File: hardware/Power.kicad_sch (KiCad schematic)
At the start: 3 parts, among them U5 BQ25798RQMR

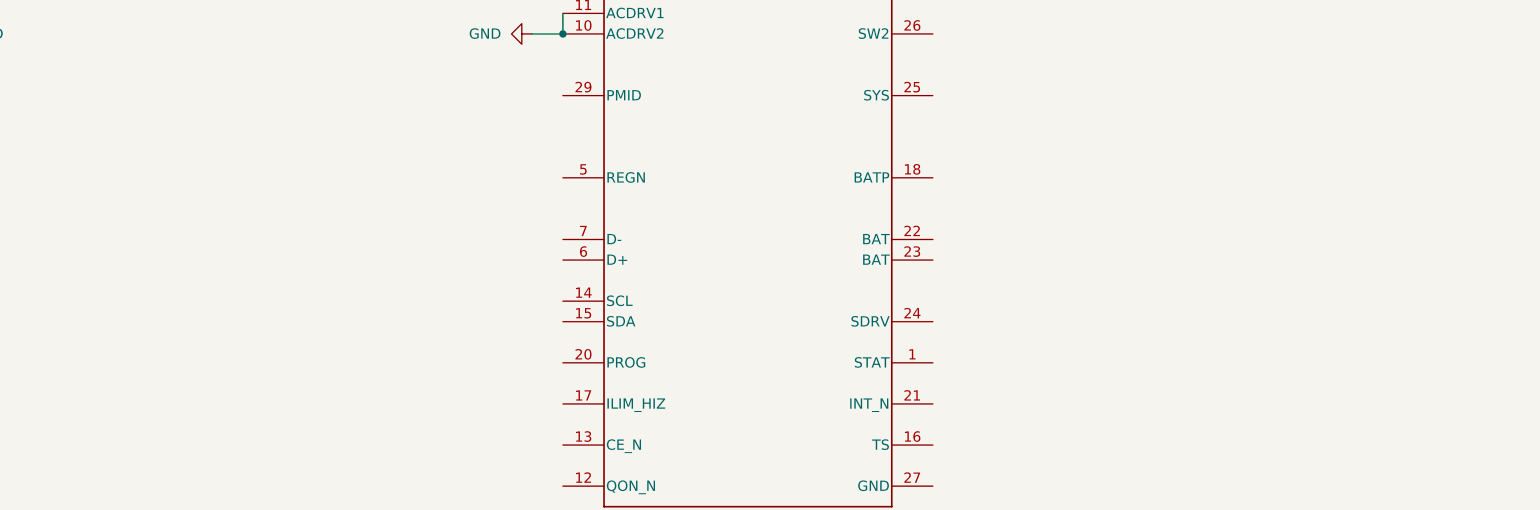
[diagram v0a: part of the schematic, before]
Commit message: Main modules added + Com lines
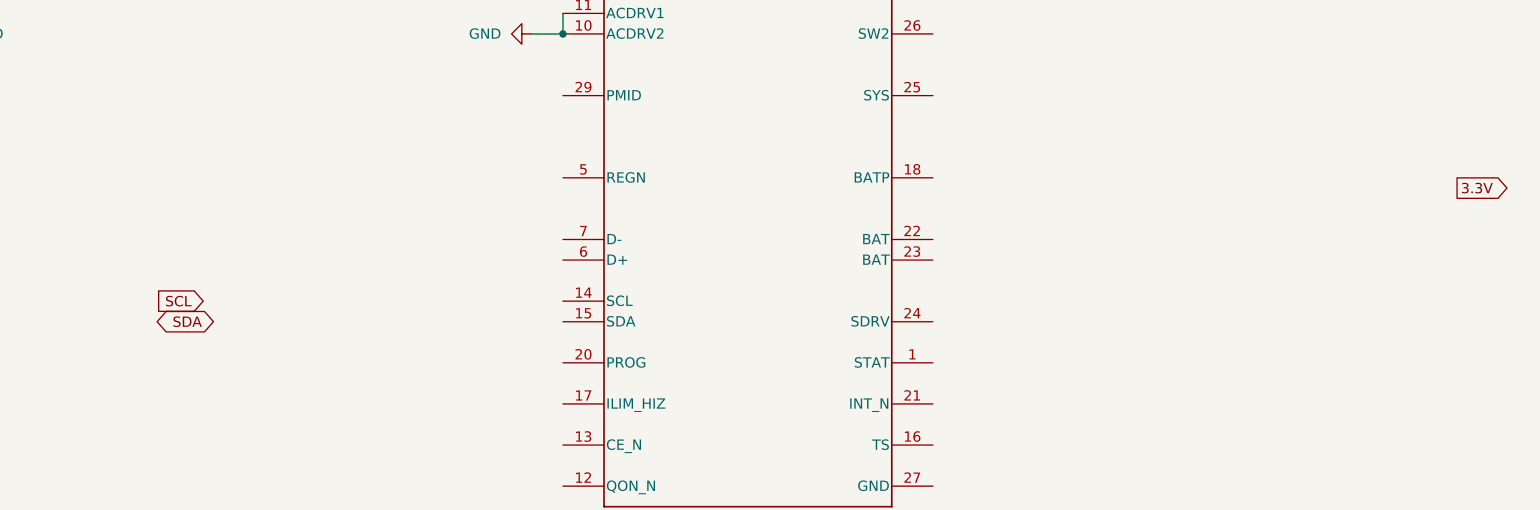
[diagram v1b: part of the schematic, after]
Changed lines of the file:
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@@
+		)
+	)
+	(global_label "3.3V"
+		(shape output)
+		(at 223.52 80.01 0)
+		(fields_autoplaced yes)
+		(effects
+			(font
+				(size 1.27 1.27)
+			)
+			(justify left)
+		)
+		(property "Intersheetrefs" "${INTERSHEET_REFS}"
+			(at 230.6176 80.01 0)
+			(effects
+				(font
+					(size 1.27 1.27)
+				)
+				(justify left)
+				(hide yes)
+			)
 		)
 	)
@@
 			(effects
 				(font
+					(size 1.27 1.27)
+				)
+				(justify right)
+				(hide yes)
+			)
+		)
+	)
+	(global_label "SCL"
+		(shape input)
+		(at 68.58 93.98 180)
+		(fields_autoplaced yes)
+		(effects
+			(font
+				(size 1.27 1.27)
+			)
+			(justify right)
+		)
+		(property "Intersheetrefs" "${INTERSHEET_REFS}"
+			(at 62.0872 93.98 0)
+			(effects
+				(font
+					(size 1.27 1.27)
+				)
+				(justify right)
+				(hide yes)
+			)
+		)
+	)
+	(global_label "SDA"
+		(shape bidirectional)
+		(at 69.85 96.52 180)
+		(fields_autoplaced yes)
+		(effects
+			(font
+				(size 1.27 1.27)
+			)
+			(justify right)
+		)
+		(property "Intersheetrefs" "${INTERSHEET_REFS}"
+			(at 62.1854 96.52 0)
+			(effects
+				(font

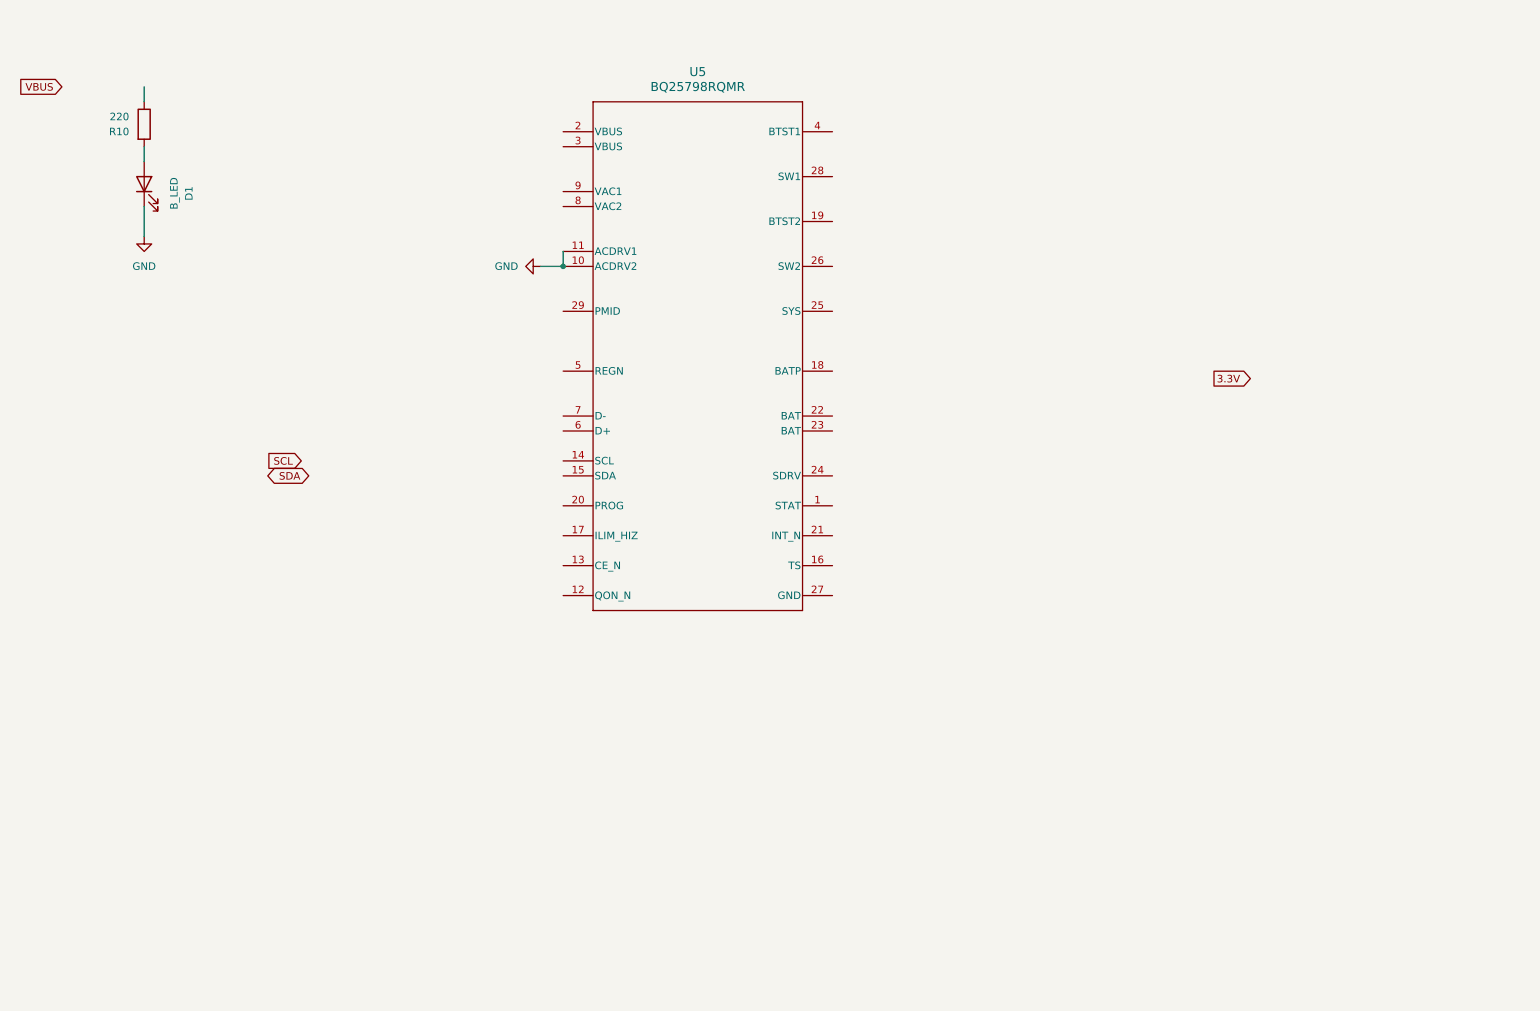
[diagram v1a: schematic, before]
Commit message: Basic 2 inputs source battery charger
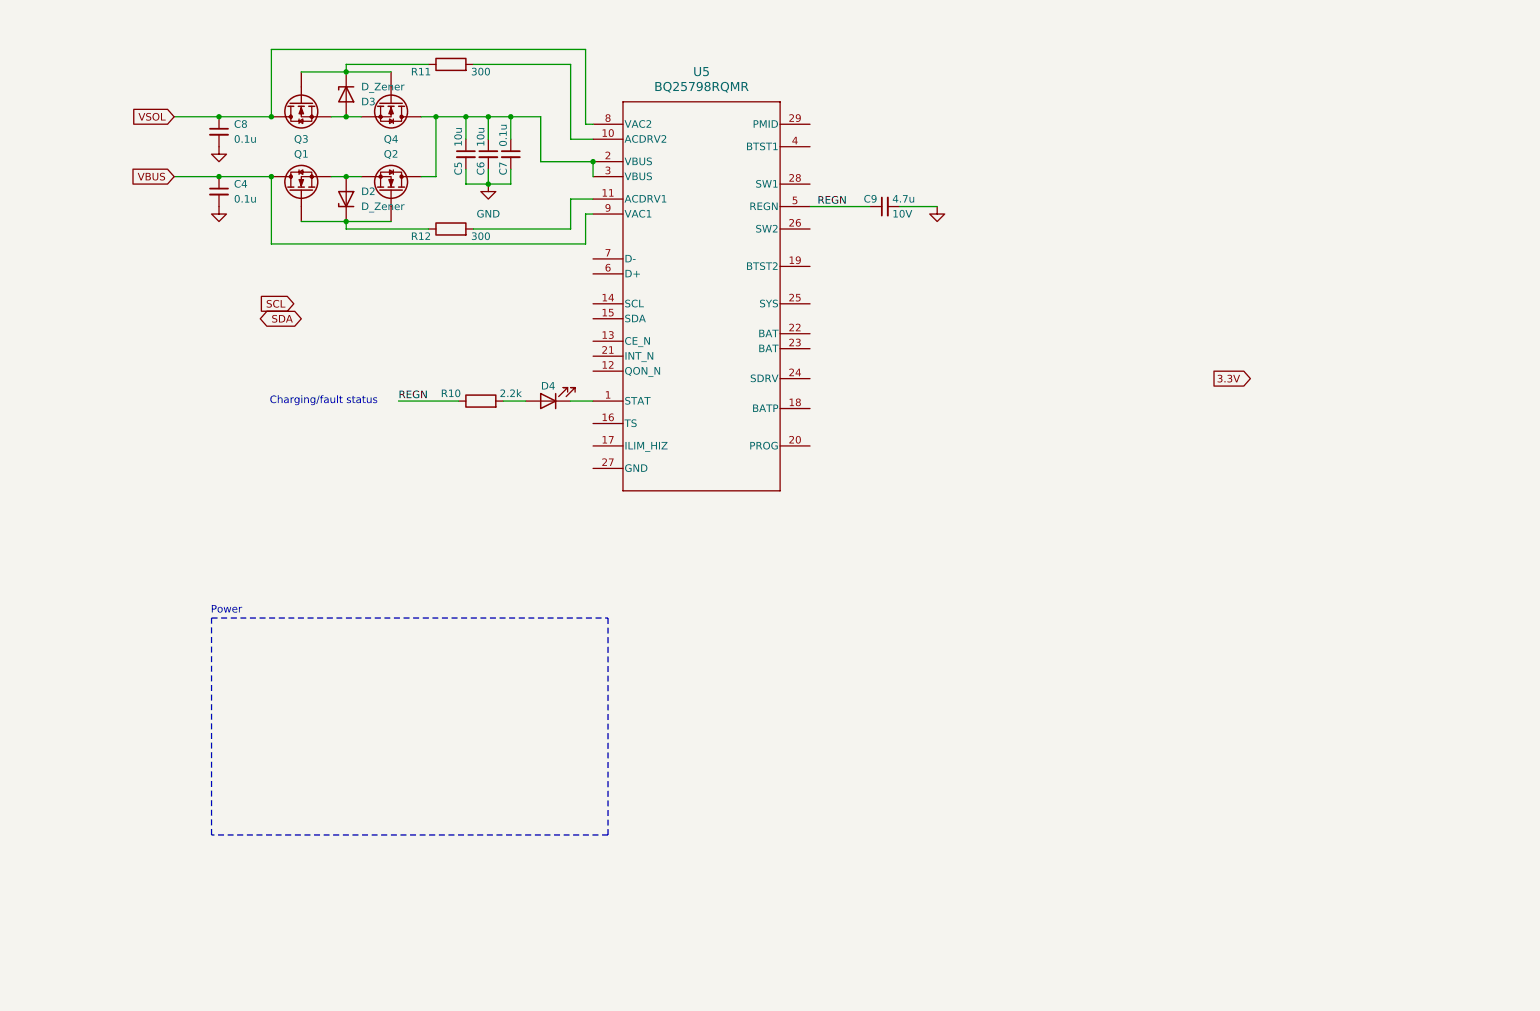
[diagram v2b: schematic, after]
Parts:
- removed D1: B_LED, LED_SMD:LED_0603_1608Metric, symbol Device:LED
- added C4, C7, C8: 0.1u, symbol Device:C_Small
- added C5, C6: 10u, symbol Device:C_Small
- added C9: 4.7u, symbol Device:C_Small
- added D2, D3: D_Zener, symbol Device:D_Zener
- added D4: LED, symbol Device:LED
- added Q1, Q2, Q3, Q4: Q_NMOS, symbol Device:Q_NMOS
- added R11, R12: 300, Resistor_SMD:R_0402_1005Metric, symbol Device:R
- R10: value 220 -> 2.2k; footprint Resistor_SMD:R_0603_1608Metric -> Resistor_SMD:R_0402_1005Metric
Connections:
- net GND: now also C4.2, C5.2, C6.2, C7.2, C8.2, C9.2; no longer U5.10 (ACDRV2), U5.11 (ACDRV1)
- net VBUS: now also U5.9 (VAC1), C4.1, Q1.D
- net at R10.2: now also D4.2 (A)
- net at U5.1 (STAT): now also D4.1 (K)
- net at U5.2 (VBUS): now also U5.3 (VBUS), C5.1, C6.1, C7.1, Q2.D, Q4.D
- net REGN: now reaches U5.5 (REGN)
- net REGN: now also R10.1, C9.1
- net VSOL: now reaches U5.8 (VAC2)
- net VSOL: now also C8.1, Q3.D
- new net: D3.1 (K), Q3.G, Q4.G, R11.1
- new net: D3.2 (A), Q3.S, Q4.S
- new net: D2.1 (K), Q1.G, Q2.G, R12.1
- new net: D2.2 (A), Q1.S, Q2.S
- new net: R11.2, U5.10 (ACDRV2)
- new net: R12.2, U5.11 (ACDRV1)
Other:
- note added: "Charging/fault status"
- note added: "Power"
- company: (none) -> ECAM
- title: (none) -> Power/Battery Management
- moved on the sheet: R10

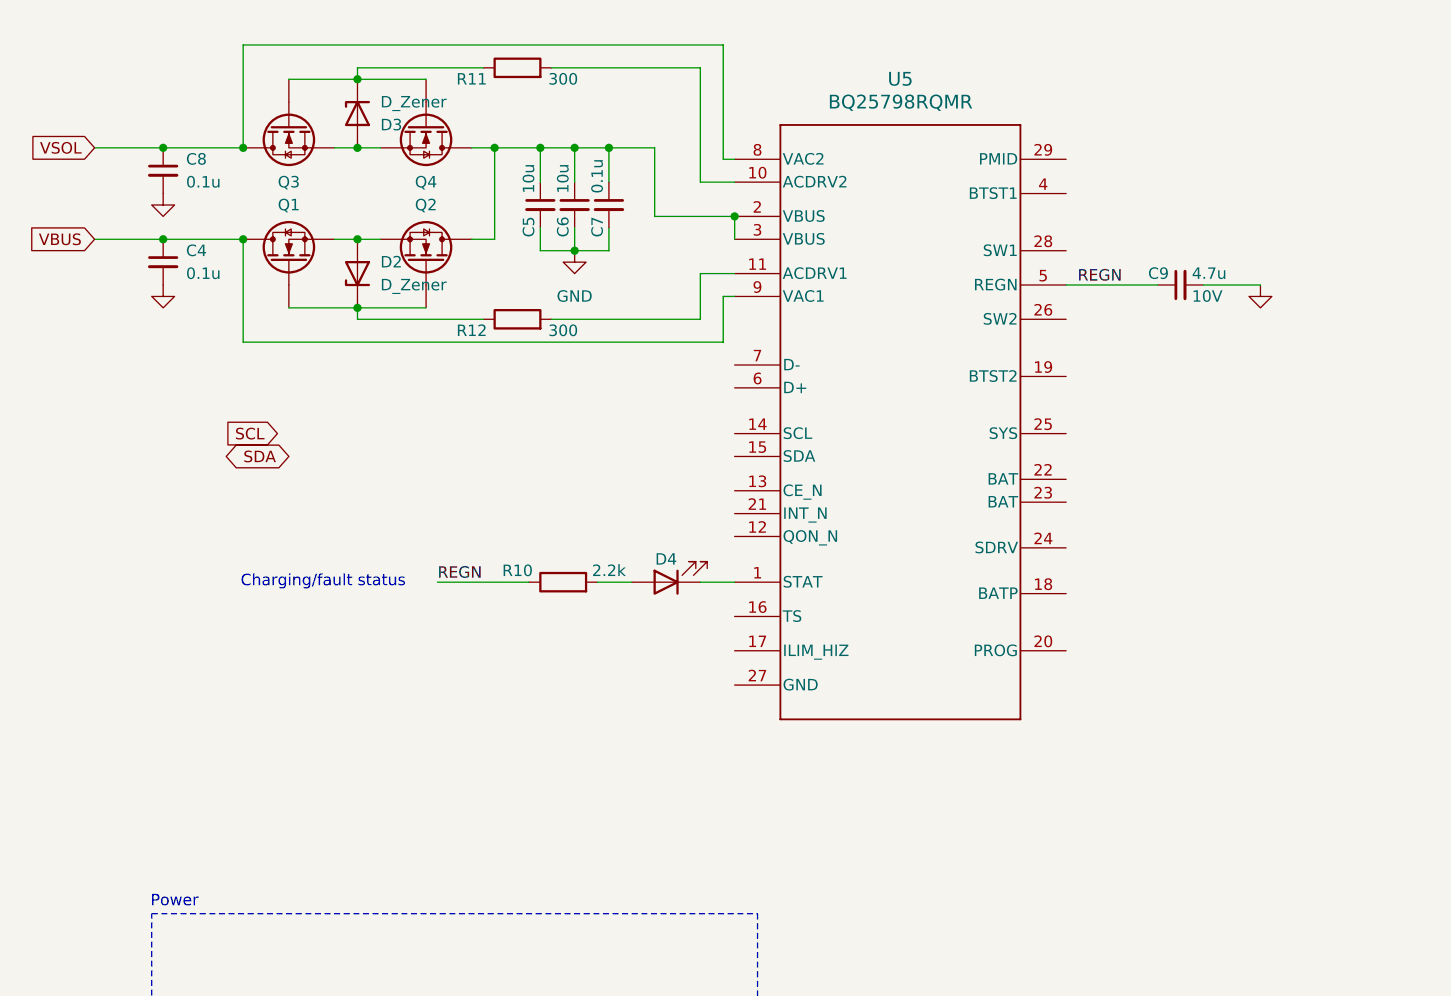
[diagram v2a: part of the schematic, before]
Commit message: Added IN current limit & switching freq
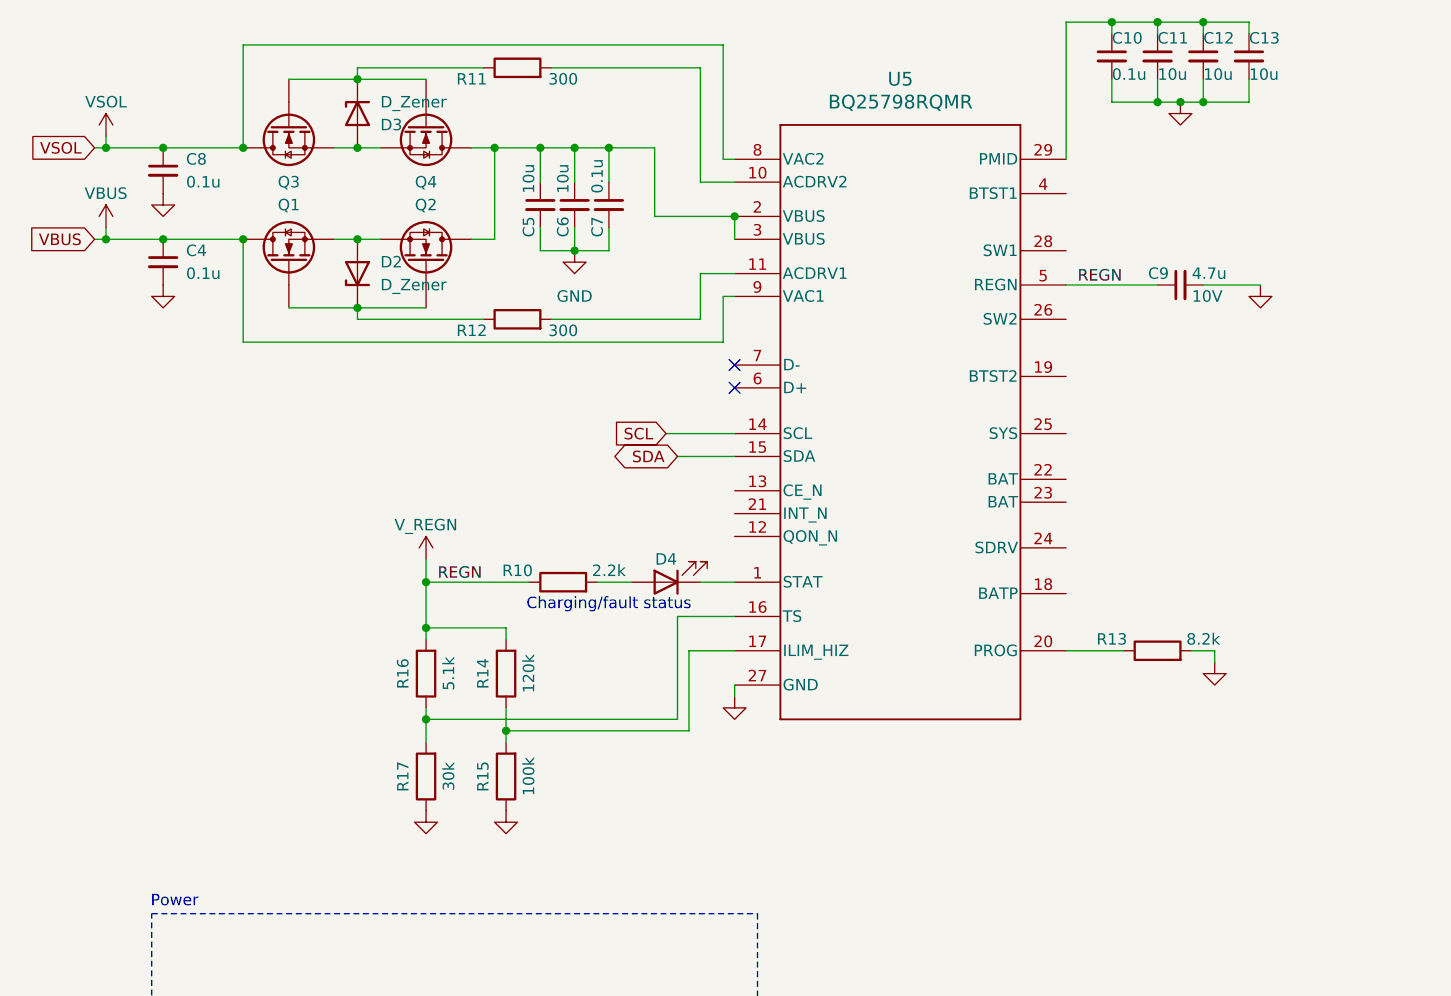
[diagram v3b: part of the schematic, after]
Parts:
- added C10: 0.1u, Capacitor_SMD:C_0402_1005Metric, symbol Device:C_Small
- added C11, C12, C13: 10u, Capacitor_SMD:C_0603_1608Metric, symbol Device:C_Small
- added R13: 8.2k, Resistor_SMD:R_0402_1005Metric, symbol Device:R
- added R14: 120k, Resistor_SMD:R_0402_1005Metric, symbol Device:R
- added R15: 100k, Resistor_SMD:R_0402_1005Metric, symbol Device:R
- added R16: 5.1k, Resistor_SMD:R_0402_1005Metric, symbol Device:R
- added R17: 30k, Resistor_SMD:R_0402_1005Metric, symbol Device:R
- C4, C7, C8: footprint (none) -> Capacitor_SMD:C_0402_1005Metric
- C5, C6, C9: footprint (none) -> Capacitor_SMD:C_0603_1608Metric
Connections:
- net GND: now also U5.27 (GND), C10.2, C11.2, C12.2, C13.2, R13.2, R15.1, R17.1
- net SCL: now also U5.14 (SCL)
- net SDA: now also U5.15 (SDA)
- net at U5.16 (TS): now also R16.1, R17.2
- net at U5.17 (ILIM_HIZ): now also R14.1, R15.2
- net at U5.20 (PROG): now also R13.1
- net at U5.29 (PMID): now also C10.1, C11.1, C12.1, C13.1
- net REGN renamed V_REGN
- net V_REGN: now also R14.2, R16.2
- no-connect marks 0 -> 2
